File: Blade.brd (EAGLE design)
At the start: 160 x 106.7 mm, 168 parts, among them IC1 THN10-2411WIR, IC10 MCP6064-E/SL, IC12 LM78L05ACMX/NOPB, IC13 CH340G, IC2 MCP6064-E/SL, IC3 MCP6064-E/SL, IC4 MCP6064-E/SL, IC5 MAX488CSA, IC6 MOCD207MSOIC-8, IC7 MOCD207MSOIC-8, IC8 MOCD207MSOIC-8, IC9 MCP6064-E/SL, Q1 12MHz, U1 ADR366WAUJZ, U10 ADS1148QPWRQ1, U11 ADS1148QPWRQ1, U12 ADS1148QPWRQ1, U13 ADR366WAUJZ, U2 ADR366WAUJZ, U3 ADS1148QPWRQ1, U4 ADS1148QPWRQ1, U5 ADS1148QPWRQ1, U6 LT1528, U7 S70FL01GS, U8 S70FL01GS, U9 STM32F77XXXLQFP208, X1 D-SUB9-H5M09RA, X2 D-SUB15-H5M15RA, X3 USBPTH

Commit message: Werte Update
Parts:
- LED1, LED2, LED3, LED4, LED5, LED6: value (none) -> 1V9
- R18: value ? -> 330
- R19: value ? -> 150
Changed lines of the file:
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@@
 <?xml version="1.0" encoding="utf-8"?>
 <!DOCTYPE eagle SYSTEM "eagle.dtd">
-<eagle version="9.2.2">
+<eagle version="9.3.1">
 <drawing>
 <settings>
-<setting alwaysvectorfont="no"/>
+<setting alwaysvectorfont="yes"/>
 <setting verticaltext="up"/>
 </settings>
@@
 <param name="tpViaShape" value="round"/>
 <param name="PrefDir.1" value="a"/>
-<param name="PrefDir.2" value="a"/>
+<param name="PrefDir.2" value="0"/>
 <param name="PrefDir.3" value="0"/>
 <param name="PrefDir.4" value="0"/>
@@
 <param name="PrefDir.13" value="0"/>
 <param name="PrefDir.14" value="0"/>
-<param name="PrefDir.15" value="a"/>
+<param name="PrefDir.15" value="0"/>
 <param name="PrefDir.16" value="a"/>
 <param name="cfVia" value="8"/>
@@
 <attribute name="VALUE" x="38.932" y="6.978" size="1.27" layer="27" rot="R90"/>
 </element>
-<element name="LED1" library="adafruit" library_urn="urn:adsk.eagle:library:420" package="CHIP-LED0603" package3d_urn="urn:adsk.eagle:package:6240556/1" value="" x="152.4" y="81.28" smashed="yes">
+<element name="LED1" library="adafruit" library_urn="urn:adsk.eagle:library:420" package="CHIP-LED0603" package3d_urn="urn:adsk.eagle:package:6240556/1" value="1V9" x="152.4" y="81.28" smashed="yes">
 <attribute name="VALUE" x="154.305" y="80.645" size="1.27" layer="27" rot="R90"/>
 </element>
-<element name="LED2" library="adafruit" library_urn="urn:adsk.eagle:library:420" package="CHIP-LED0603" package3d_urn="urn:adsk.eagle:package:6240556/1" value="" x="154.305" y="81.28" smashed="yes">
+<element name="LED2" library="adafruit" library_urn="urn:adsk.eagle:library:420" package="CHIP-LED0603" package3d_urn="urn:adsk.eagle:package:6240556/1" value="1V9" x="154.305" y="81.28" smashed="yes">
 <attribute name="VALUE" x="156.21" y="80.645" size="1.27" layer="27" rot="R90"/>
 </element>
-<element name="LED3" library="adafruit" library_urn="urn:adsk.eagle:library:420" package="CHIP-LED0603" package3d_urn="urn:adsk.eagle:package:6240556/1" value="" x="156.21" y="81.28" smashed="yes">
+<element name="LED3" library="adafruit" library_urn="urn:adsk.eagle:library:420" package="CHIP-LED0603" package3d_urn="urn:adsk.eagle:package:6240556/1" value="1V9" x="156.21" y="81.28" smashed="yes">
 <attribute name="VALUE" x="158.115" y="80.645" size="1.27" layer="27" rot="R90"/>
 </element>
-<element name="LED4" library="adafruit" library_urn="urn:adsk.eagle:library:420" package="CHIP-LED0603" package3d_urn="urn:adsk.eagle:package:6240556/1" value="" x="158.115" y="81.28" smashed="yes">
+<element name="LED4" library="adafruit" library_urn="urn:adsk.eagle:library:420" package="CHIP-LED0603" package3d_urn="urn:adsk.eagle:package:6240556/1" value="1V9" x="158.115" y="81.28" smashed="yes">
 <attribute name="VALUE" x="160.02" y="80.645" size="1.27" layer="27" rot="R90"/>
 </element>
@@
 <attribute name="VALUE" x="123.19" y="43.815" size="1.27" layer="27"/>
 </element>
-<element name="LED5" library="adafruit" library_urn="urn:adsk.eagle:library:420" package="CHIP-LED0603" package3d_urn="urn:adsk.eagle:package:6240556/1" value="" x="150.495" y="81.28" smashed="yes">
+<element name="LED5" library="adafruit" library_urn="urn:adsk.eagle:library:420" package="CHIP-LED0603" package3d_urn="urn:adsk.eagle:package:6240556/1" value="1V9" x="150.495" y="81.28" smashed="yes">
 <attribute name="VALUE" x="152.4" y="80.645" size="1.27" layer="27" rot="R90"/>
 </element>
-<element name="LED6" library="adafruit" library_urn="urn:adsk.eagle:library:420" package="CHIP-LED0603" package3d_urn="urn:adsk.eagle:package:6240556/1" value="" x="148.59" y="81.28" smashed="yes">
+<element name="LED6" library="adafruit" library_urn="urn:adsk.eagle:library:420" package="CHIP-LED0603" package3d_urn="urn:adsk.eagle:package:6240556/1" value="1V9" x="148.59" y="81.28" smashed="yes">
 <attribute name="VALUE" x="150.495" y="80.645" size="1.27" layer="27" rot="R90"/>
 </element>
-<element name="R18" library="rcl" library_urn="urn:adsk.eagle:library:334" package="R0805" package3d_urn="urn:adsk.eagle:package:23553/2" value="?" x="150.495" y="82.296" smashed="yes" rot="MR90">
+<element name="R18" library="rcl" library_urn="urn:adsk.eagle:library:334" package="R0805" package3d_urn="urn:adsk.eagle:package:23553/2" value="330" x="150.495" y="82.296" smashed="yes" rot="MR90">
 <attribute name="NAME" x="153.162" y="83.947" size="1.27" layer="26" rot="MR270"/>
 <attribute name="POPULARITY" value="86" x="150.495" y="82.296" size="1.778" layer="28" rot="MR90" display="off"/>
@@
 <attribute name="VALUE" x="147.955" y="81.661" size="1.27" layer="28" rot="MR90"/>
 </element>
-<element name="R19" library="rcl" library_urn="urn:adsk.eagle:library:334" package="R0805" package3d_urn="urn:adsk.eagle:package:23553/2" value="?" x="147.828" y="82.296" smashed="yes" rot="MR90">
+<element name="R19" library="rcl" library_urn="urn:adsk.eagle:library:334" package="R0805" package3d_urn="urn:adsk.eagle:package:23553/2" value="150" x="147.828" y="82.296" smashed="yes" rot="MR90">
 <attribute name="NAME" x="149.733" y="84.963" size="1.27" layer="26" rot="MR0"/>
 <attribute name="POPULARITY" value="86" x="147.828" y="82.296" size="1.778" layer="28" rot="MR90" display="off"/>

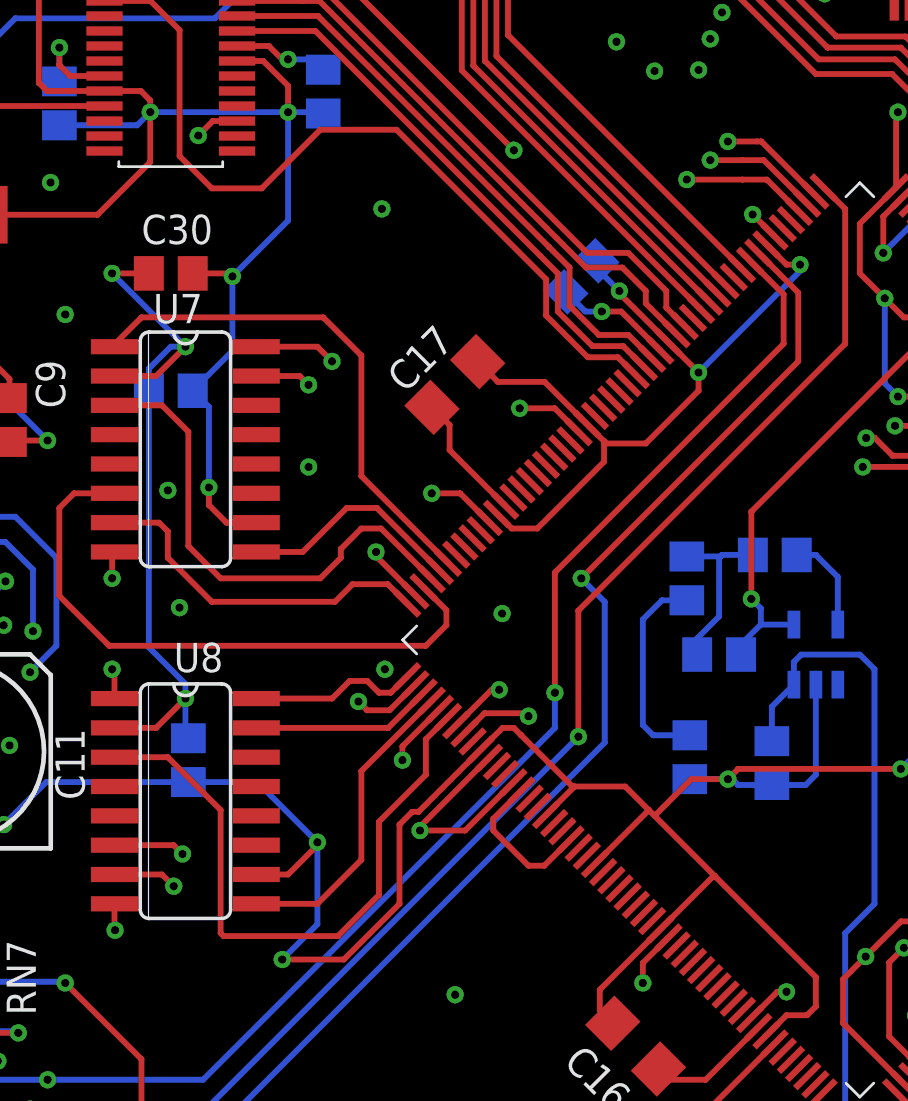
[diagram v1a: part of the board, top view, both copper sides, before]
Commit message: flash footprint korrigiert
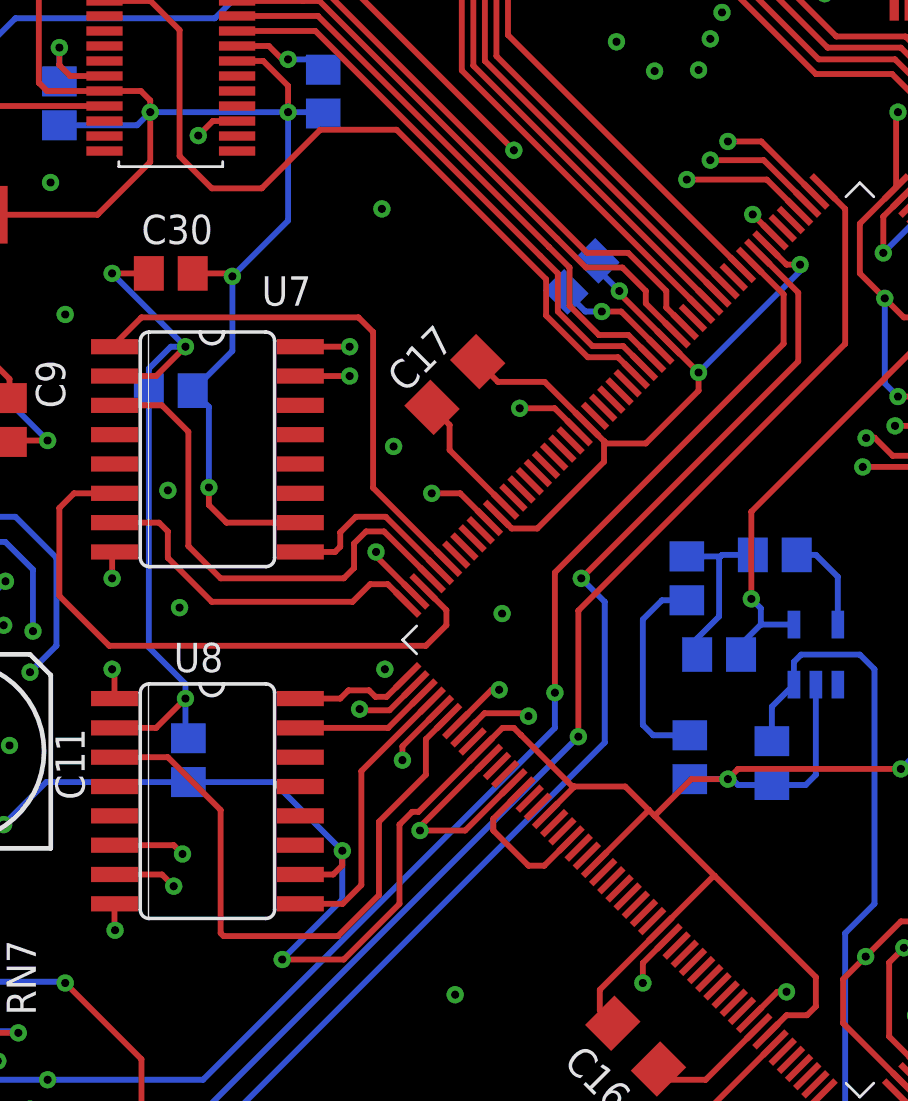
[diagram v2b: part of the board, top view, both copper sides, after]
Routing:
- net GND: track 1473.7 -> 1476.3 mm
- net SPI6_SCK: track 29.4 -> 27.0 mm
- net SPI6_MOSI: track 27.9 -> 25.7 mm
- net SPI2_SCK: track 7.36 -> 5.26 mm
- net SPI2_MOSI: track 7.88 -> 5.97 mm
- net FL_1_WP: track 9.87 -> 8.01 mm
- net FL_2_WP: track 13.5 -> 12.2 mm
- net FL_1_HLD: track 22.5 -> 23.4 mm

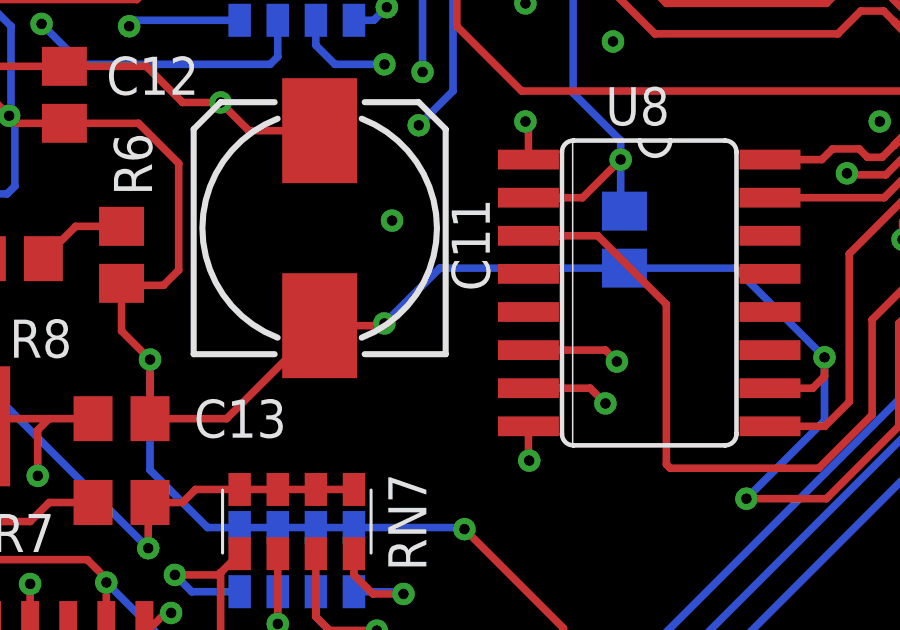
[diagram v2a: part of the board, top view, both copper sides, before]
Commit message: led widerstand angepasst
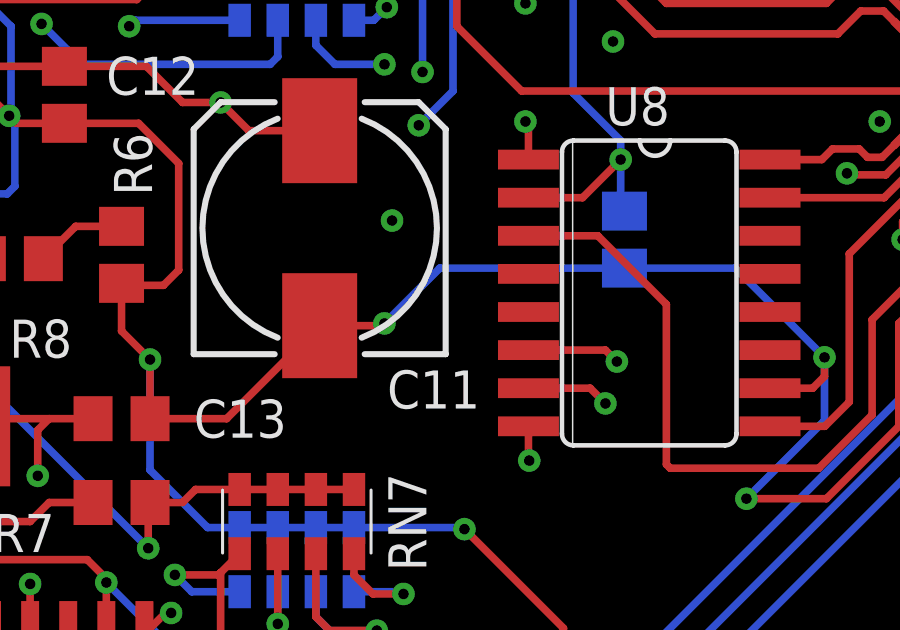
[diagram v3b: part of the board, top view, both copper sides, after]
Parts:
- R18: value 330 -> 680
- R19: value 150 -> 330
- RN10: value 270 -> 330
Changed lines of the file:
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@@
 </element>
 <element name="C11" library="rcl" library_urn="urn:adsk.eagle:library:334" package="153CLV-0810" package3d_urn="urn:adsk.eagle:package:23401/2" value="4u7" x="29.337" y="32.639" smashed="yes" rot="R90">
-<attribute name="NAME" x="33.74" y="33.627" size="1.27" layer="25" rot="R270"/>
+<attribute name="NAME" x="31.5875" y="26.628" size="1.27" layer="25"/>
 <attribute name="SPICEPREFIX" value="C" x="29.337" y="13.589" size="1.778" layer="27" rot="R90" display="off"/>
 <attribute name="VALUE" x="35.122" y="28.314" size="1.27" layer="27" rot="R90"/>
@@
 <attribute name="VALUE" x="160.02" y="80.645" size="1.27" layer="27" rot="R90"/>
 </element>
-<element name="RN10" library="resistor-dil" library_urn="urn:adsk.eagle:library:342" package="EXBS8V" package3d_urn="urn:adsk.eagle:package:24925/1" value="270" x="134.62" y="72.39" smashed="yes" rot="R270">
+<element name="RN10" library="resistor-dil" library_urn="urn:adsk.eagle:library:342" package="EXBS8V" package3d_urn="urn:adsk.eagle:package:24925/1" value="330" x="134.62" y="72.39" smashed="yes" rot="R270">
 <attribute name="MF" value="" x="134.62" y="72.39" size="1.778" layer="27" rot="R270" display="off"/>
 <attribute name="MPN" value="" x="134.62" y="72.39" size="1.778" layer="27" rot="R270" display="off"/>
@@
 <attribute name="VALUE" x="150.495" y="80.645" size="1.27" layer="27" rot="R90"/>
 </element>
-<element name="R18" library="rcl" library_urn="urn:adsk.eagle:library:334" package="R0805" package3d_urn="urn:adsk.eagle:package:23553/2" value="330" x="150.495" y="82.296" smashed="yes" rot="MR90">
+<element name="R18" library="rcl" library_urn="urn:adsk.eagle:library:334" package="R0805" package3d_urn="urn:adsk.eagle:package:23553/2" value="680" x="150.495" y="82.296" smashed="yes" rot="MR90">
 <attribute name="NAME" x="153.162" y="83.947" size="1.27" layer="26" rot="MR270"/>
 <attribute name="SPICEPREFIX" value="R" x="150.495" y="82.296" size="1.778" layer="28" rot="MR90" display="off"/>
 <attribute name="VALUE" x="147.955" y="81.661" size="1.27" layer="28" rot="MR90"/>
 </element>
-<element name="R19" library="rcl" library_urn="urn:adsk.eagle:library:334" package="R0805" package3d_urn="urn:adsk.eagle:package:23553/2" value="150" x="147.828" y="82.296" smashed="yes" rot="MR90">
+<element name="R19" library="rcl" library_urn="urn:adsk.eagle:library:334" package="R0805" package3d_urn="urn:adsk.eagle:package:23553/2" value="330" x="147.828" y="82.296" smashed="yes" rot="MR90">
 <attribute name="NAME" x="149.733" y="84.963" size="1.27" layer="26" rot="MR0"/>
 <attribute name="SPICEPREFIX" value="R" x="147.828" y="82.296" size="1.778" layer="28" rot="MR90" display="off"/>

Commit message: Widerstände Wert definiert
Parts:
- R20: value ? -> 4k7
- R21: value ? -> 470
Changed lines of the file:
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@@
 <attribute name="VALUE" x="157.48" y="36.195" size="1.27" layer="27" rot="R90"/>
 </element>
-<element name="R20" library="rcl" library_urn="urn:adsk.eagle:library:334" package="R0805" package3d_urn="urn:adsk.eagle:package:23553/2" value="?" x="150.876" y="35.687" smashed="yes" rot="MR0">
+<element name="R20" library="rcl" library_urn="urn:adsk.eagle:library:334" package="R0805" package3d_urn="urn:adsk.eagle:package:23553/2" value="4k7" x="150.876" y="35.687" smashed="yes" rot="MR0">
 <attribute name="NAME" x="154.94" y="36.449" size="1.27" layer="26" rot="MR180"/>
 <attribute name="SPICEPREFIX" value="R" x="150.876" y="35.687" size="1.778" layer="28" rot="MR0" display="off"/>
@@
 <attribute name="VALUE" x="155.575" y="36.195" size="1.27" layer="27" rot="R90"/>
 </element>
-<element name="R21" library="rcl" library_urn="urn:adsk.eagle:library:334" package="R0805" package3d_urn="urn:adsk.eagle:package:23553/2" value="?" x="150.876" y="37.719" smashed="yes" rot="MR0">
+<element name="R21" library="rcl" library_urn="urn:adsk.eagle:library:334" package="R0805" package3d_urn="urn:adsk.eagle:package:23553/2" value="470" x="150.876" y="37.719" smashed="yes" rot="MR0">
 <attribute name="NAME" x="153.416" y="38.735" size="1.27" layer="26" rot="MR180"/>
 <attribute name="SPICEPREFIX" value="R" x="150.876" y="37.719" size="1.778" layer="28" rot="MR0" display="off"/>
